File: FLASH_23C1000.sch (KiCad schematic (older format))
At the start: 8 parts, among them J1 uPD23C1000 / FLASH, U1 29F010 TSOP-32 20mm, U2 29F010 sTSOP-32 14mm, U3 29F010 PLCC 7x9

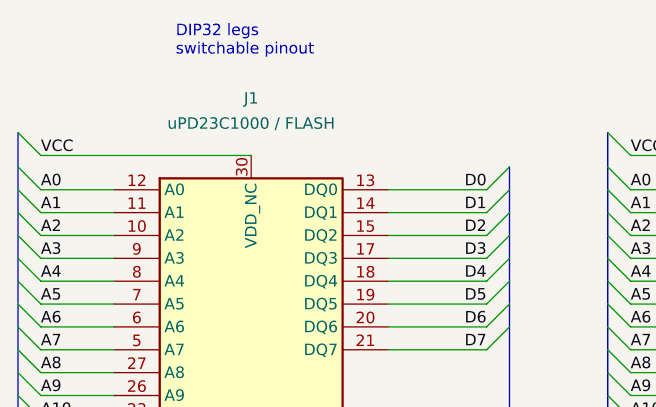
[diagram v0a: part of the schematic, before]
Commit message: Rename FlashROM_8300 to FLASH_23C1000
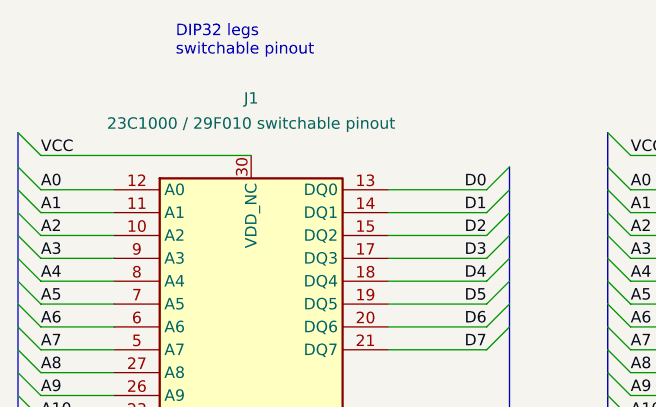
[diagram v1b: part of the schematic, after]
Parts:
- J1: value uPD23C1000 / FLASH -> 23C1000 / 29F010 switchable pinout
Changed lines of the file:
@@
 encoding utf-8
 Sheet 1 1
-Title "Flash-based uPD23C1000 replacement"
-Date "2021-03-07"
+Title "29F010 to 23C1000"
+Date "2021-05-09"
 Rev "002"
 Comp "Brian K. White - b.kenyon.w@gmail.com"
-Comment1 "DIP-32 version"
+Comment1 ""
 Comment2 ""
 Comment3 ""
@@
 P 2190 3500
 F 0 "J1" H 2190 5100 50  0000 C CNN
-F 1 "uPD23C1000 / FLASH" H 2190 4990 50  0000 C CNN
+F 1 "23C1000 / 29F010 switchable pinout" H 2190 4990 50  0000 C CNN
 F 2 "000_LOCAL:DIP32_0.6_pcb_sil_pins" H 2190 3500 50  0001 C CNN
 F 3 "http://ww1.microchip.com/downloads/en/DeviceDoc/doc0014.pdf" H 2190 3500 50  0001 C CNN
